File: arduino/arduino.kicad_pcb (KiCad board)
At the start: 2 copper layers, 45.7 x 45.7 mm, 17 parts, among them IC1 ATMEGA328P-P, P1 CONN_6, P2 CONN_6, Q1 16MHz

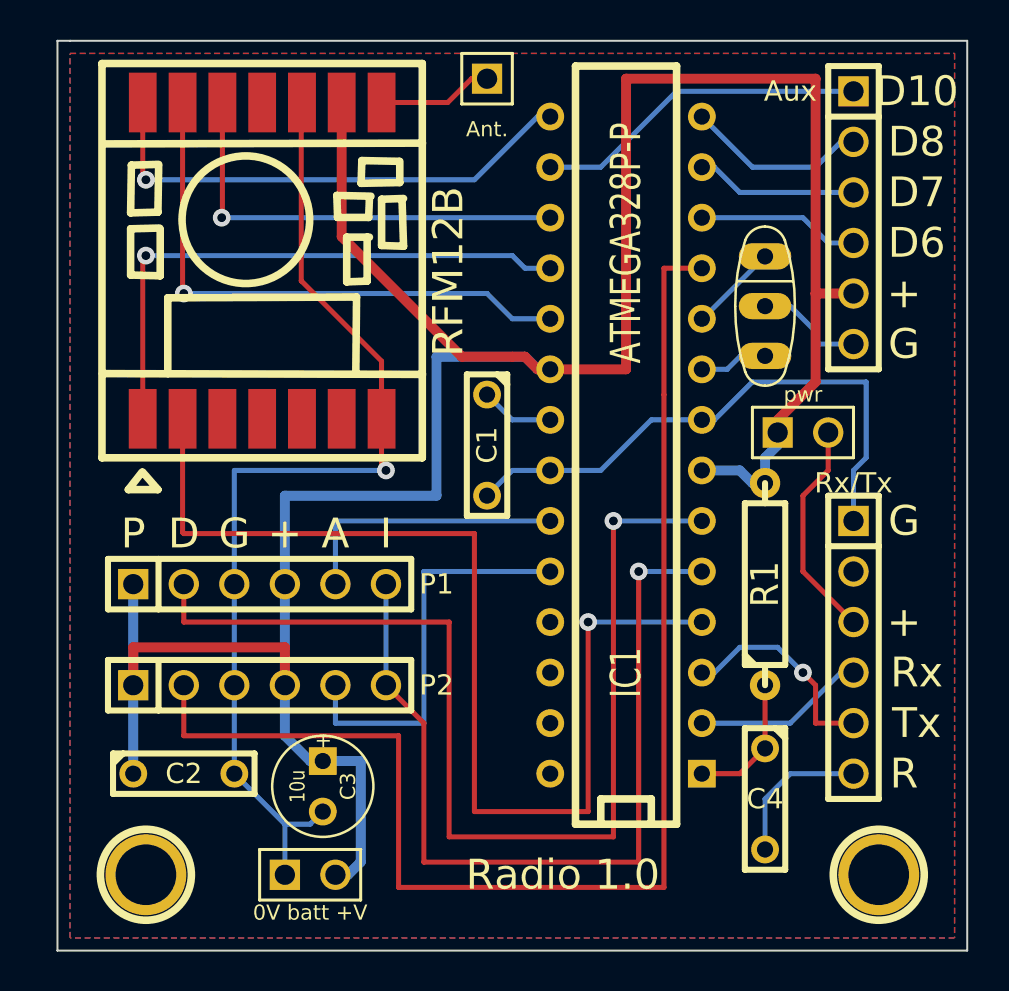
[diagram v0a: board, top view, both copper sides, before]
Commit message: swap pins 15/16 on cpu
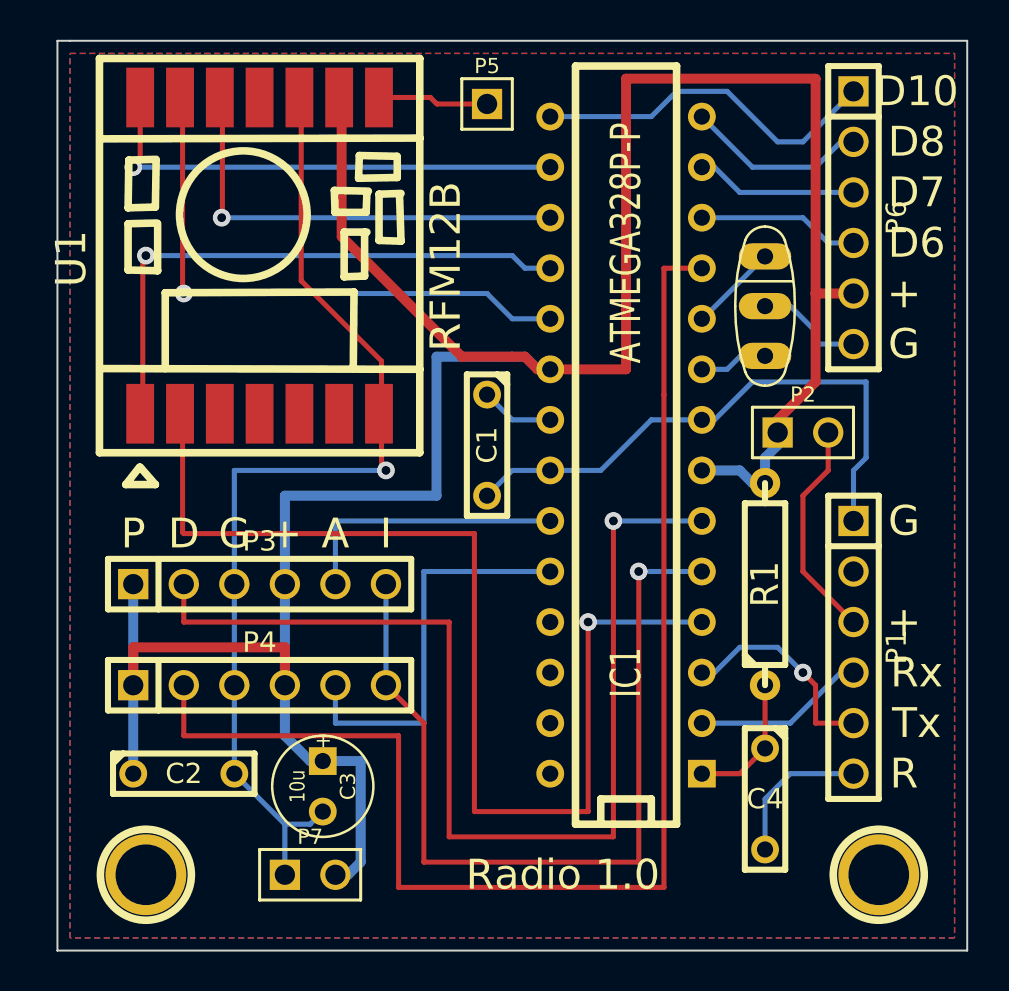
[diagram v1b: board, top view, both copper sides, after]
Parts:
- removed 0V batt +V: battery, PIN_ARRAY_2X1
- removed the ? at (81.4, 123.4)
- removed Ant.: CONN_1, PIN_ARRAY_1
- removed Aux, Rx/Tx: CONN_6, PIN_ARRAY-6X1
- removed pwr: CONN_2, PIN_ARRAY_2X1
- added P3: CONN_6, PIN_ARRAY-6X1, F.Cu at (81.3, 139.7)
- added P4: CONN_6, PIN_ARRAY-6X1, F.Cu at (81.3, 144.8)
- added P5: CONN_1, PIN_ARRAY_1, F.Cu at (92.7, 115.6)
- added P6: CONN_6, PIN_ARRAY-6X1, F.Cu at (111.1, 121.3)
- added P7: battery, PIN_ARRAY_2X1, F.Cu at (83.8, 154.3)
- added U1: RFM12B, SMD-RFM12B, F.Cu at (81.3, 123.2)
- P2: value CONN_6 -> CONN_2; footprint PIN_ARRAY-6X1 -> PIN_ARRAY_2X1
- moved P2 30.1 mm to (108.6, 132.1)
- moved P1 30.0 mm to (111.1, 142.9), turned to 270 degrees
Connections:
- C4 pad 2: N-0000033 -> N-0000034
- IC1 pad 11: N-000008 -> N-000007
- IC1 pad 2: N-0000034 -> N-0000028
- IC1 pad 24: N-000004 -> N-000005
- IC1 pad 5: N-0000011 (its old number) -> N-0000010
- IC1 pad 6: N-000005 -> N-000004
- P1 pad 1: VCC -> GND
- P1 pad 2: N-000005 -> (no net)
- P1 pad 3: GND -> N-0000020
- P1 pad 4: VCC -> N-0000028
- P1 pad 5: N-000006 -> N-0000027
- P1 pad 6: N-0000011 (its old number) -> N-0000034
- P2 pad 2: N-000008 -> N-0000020
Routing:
- net N-000008: track 67.3 -> 0.00 mm
- net N-000007: track 0.00 -> 67.3 mm
- net N-0000011 (its old number): track 43.3 -> 0.00 mm, vias 1 -> 0
- net N-000005: track 54.6 -> 20.3 mm, vias 1 -> 0
- net N-000004: track 20.3 -> 54.6 mm, vias 0 -> 1
- net N-0000010: track 11.1 -> 43.3 mm, vias 0 -> 1
- net N-0000020: track 0.00 -> 11.1 mm
- net N-0000028: track 0.00 -> 8.67 mm
- net N-0000015: track 16.8 -> 24.6 mm, vias 0 -> 1
- net N-0000011: track 25.6 -> 17.9 mm, vias 1 -> 0
- net N-0000033: track 7.51 -> 0.00 mm
- net N-0000034: track 8.67 -> 7.51 mm

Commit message: fix port labels
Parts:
- 0 batt +: renamed from P7
- renumbered U1 to ?, P5 to Ant., P6 to Aux., P3 to P1, P4 to P2, P1 to Rx/Tx, P2 to pwr
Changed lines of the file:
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@@
   (module SMD-RFM12B (layer F.Cu)
     (at 81.28 123.19 270)
-    (fp_text reference U1 (at 0.1524 9.46912 270) (layer F.SilkS)
+    (fp_text reference "" (at 0.1524 9.46912 270) (layer F.SilkS)
       (effects (font (size 1.524 1.524) (thickness 0.3048)))
     )
@@
     (descr "Connecteurs 2 pins")
     (tags "CONN DEV")
-    (fp_text reference P7 (at 0 -1.905) (layer F.SilkS)
+    (fp_text reference "0 batt +" (at 0 1.905) (layer F.SilkS)
       (effects (font (size 0.762 0.762) (thickness 0.1524)))
     )
@@
     (descr "1 pin")
     (tags "CONN DEV")
-    (fp_text reference P5 (at 0 -1.905) (layer F.SilkS)
+    (fp_text reference Ant. (at 0 1.905) (layer F.SilkS)
       (effects (font (size 0.762 0.762) (thickness 0.1524)))
     )
@@
     (descr "Connecteur 6 pins")
     (tags "CONN DEV")
-    (fp_text reference P3 (at 0 -2.159) (layer F.SilkS)
+    (fp_text reference P1 (at 9.525 0) (layer F.SilkS)
       (effects (font (size 1.016 1.016) (thickness 0.2032)))
     )
@@
     (descr "Connecteur 6 pins")
     (tags "CONN DEV")
-    (fp_text reference P4 (at 0 -2.159) (layer F.SilkS)
+    (fp_text reference P2 (at 9.525 0) (layer F.SilkS)
       (effects (font (size 1.016 1.016) (thickness 0.2032)))
     )
@@
     (descr "Connecteur 6 pins")
     (tags "CONN DEV")
-    (fp_text reference P6 (at 0 -2.159 270) (layer F.SilkS)
+    (fp_text reference Aux. (at -6.35 3.175 360) (layer F.SilkS)
       (effects (font (size 1.016 1.016) (thickness 0.2032)))
     )
@@
     (descr "Connecteurs 2 pins")
     (tags "CONN DEV")
-    (fp_text reference P2 (at 0 -1.905) (layer F.SilkS)
+    (fp_text reference pwr (at 0 -1.905) (layer F.SilkS)
       (effects (font (size 0.762 0.762) (thickness 0.1524)))
     )
@@
     (descr "Connecteur 6 pins")
     (tags "CONN DEV")
-    (fp_text reference P1 (at 0 -2.159 270) (layer F.SilkS)
+    (fp_text reference Rx/Tx (at -8.89 -1.905 360) (layer F.SilkS)
       (effects (font (size 1.016 1.016) (thickness 0.2032)))
     )
@@
   (segment (start 79.375 121.285) (end 79.40802 121.25198) (width 0.254) (layer F.Cu) (net 12))
   (via (at 79.375 121.285) (size 0.889) (layers F.Cu B.Cu) (net 12))
-  (segment (start 87.27948 115.24234) (end 89.86266 115.24234) (width 0.254) (layer F.Cu) (net 13) (status 400000))
-  (segment (start 90.19032 115.57) (end 92.71 115.57) (width 0.254) (layer F.Cu) (net 13) (status 800000))
+  (segment (start 87.27948 115.24234) (end 89.86266 115.24234) (width 0.254) (layer F.Cu) (net 13))
+  (segment (start 90.19032 115.57) (end 92.71 115.57) (width 0.254) (layer F.Cu) (net 13))
   (segment (start 89.86266 115.24234) (end 90.19032 115.57) (width 0.254) (layer F.Cu) (net 13))
   (segment (start 103.505 141.605) (end 97.79 141.605) (width 0.254) (layer B.Cu) (net 14))
